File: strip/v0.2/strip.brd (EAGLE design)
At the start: 71 x 12 mm, 96 parts, among them IC1 LP2992, IC2 AUIRS2184S, IC3 MAX3051, IC4 OPA335, IC5 AUIRS2184S, IC6 AUIRS2184S, IC7 STM32F050CX, Q1 IRF7828, Q2 IRF7828, Q3 IRF7828, Q4 IRF7828, Q5 IRF7828, Q6 IRF7828

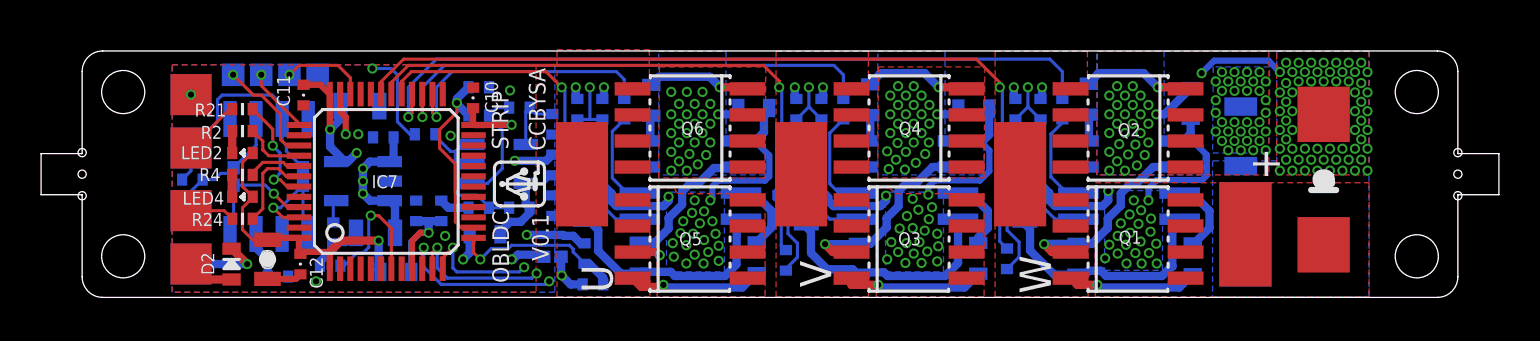
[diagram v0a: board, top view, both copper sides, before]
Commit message: Updated bootstrap circuit.
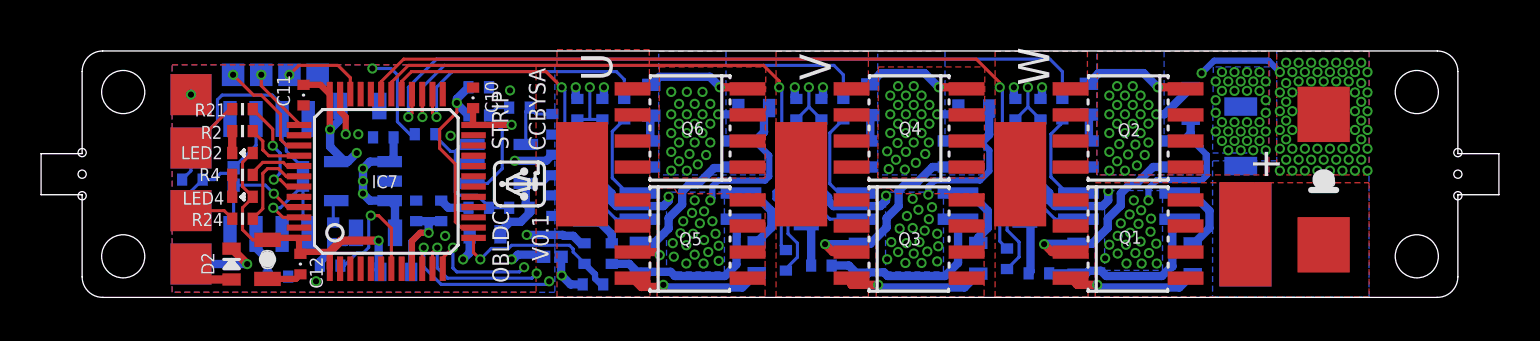
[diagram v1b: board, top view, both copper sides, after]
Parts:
- added R52, R53, R54: 2R, pel_dipol_comp:0402-RES
- D1, D3: value BAS21 -> BAT46WH
- R46, R47, R48, R49, R50, R51: value 10R -> 5R
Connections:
- new net N$1: D1.C, R52.P$2
- new net N$2: D4.C, R54.P$2
- new net N$3: D3.C, R53.P$2
- net U_VB: now also R52.P$1; no longer D1.C
- net V_VB: now also R53.P$1; no longer D3.C
- net W_VB: now also R54.P$1; no longer D4.C
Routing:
- net W_VB: track 12.2 -> 8.86 mm
- net V_VB: track 11.9 -> 8.98 mm
- net N$2: track 0.00 -> 2.83 mm
- net U_VB: track 11.8 -> 9.03 mm
- net N$3: track 0.00 -> 2.26 mm
- net N$1: track 0.00 -> 2.09 mm

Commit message: Updated bootstrap circuit
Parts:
- C23, C24, C25: value 1u -> 100nF
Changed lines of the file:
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@@
 <attribute name="PARTNO" value="*" x="20.5232" y="5.5332" size="1.778" layer="28" rot="MR90" display="off"/>
 </element>
-<element name="C23" library="pel_dipol_comp" package="0603-CAP" value="1u" x="23.114" y="1.909" smashed="yes" rot="MR90">
+<element name="C23" library="pel_dipol_comp" package="0603-CAP" value="100nF" x="23.114" y="1.909" smashed="yes" rot="MR90">
 <attribute name="NAME" x="23.5966" y="0.9438" size="0.635" layer="26" font="vector" ratio="16" rot="MR90"/>
 <attribute name="VALUE" x="21.59" y="0.7914" size="0.635" layer="28" font="vector" ratio="16" rot="MR90"/>
@@
 <attribute name="PARTNO" value="*" x="31.2674" y="5.3554" size="1.778" layer="28" rot="MR90" display="off"/>
 </element>
-<element name="C24" library="pel_dipol_comp" package="0603-CAP" value="1u" x="33.782" y="1.8582" smashed="yes" rot="MR90">
+<element name="C24" library="pel_dipol_comp" package="0603-CAP" value="100nF" x="33.782" y="1.8582" smashed="yes" rot="MR90">
 <attribute name="NAME" x="34.1884" y="0.893" size="0.635" layer="26" font="vector" ratio="16" rot="MR90"/>
 <attribute name="VALUE" x="32.258" y="0.7406" size="0.635" layer="28" font="vector" ratio="16" rot="MR90"/>
@@
 <attribute name="PARTNO" value="*" x="41.91" y="5.4824" size="1.778" layer="28" rot="MR90" display="off"/>
 </element>
-<element name="C25" library="pel_dipol_comp" package="0603-CAP" value="1u" x="44.4246" y="1.8582" smashed="yes" rot="MR90">
+<element name="C25" library="pel_dipol_comp" package="0603-CAP" value="100nF" x="44.4246" y="1.8582" smashed="yes" rot="MR90">
 <attribute name="NAME" x="44.9072" y="0.9692" size="0.635" layer="26" font="vector" ratio="16" rot="MR90"/>
 <attribute name="VALUE" x="42.9006" y="0.7406" size="0.635" layer="28" font="vector" ratio="16" rot="MR90"/>
@@
 </signal>
 </signals>
-<errors>
-</errors>
 </board>
 </drawing>

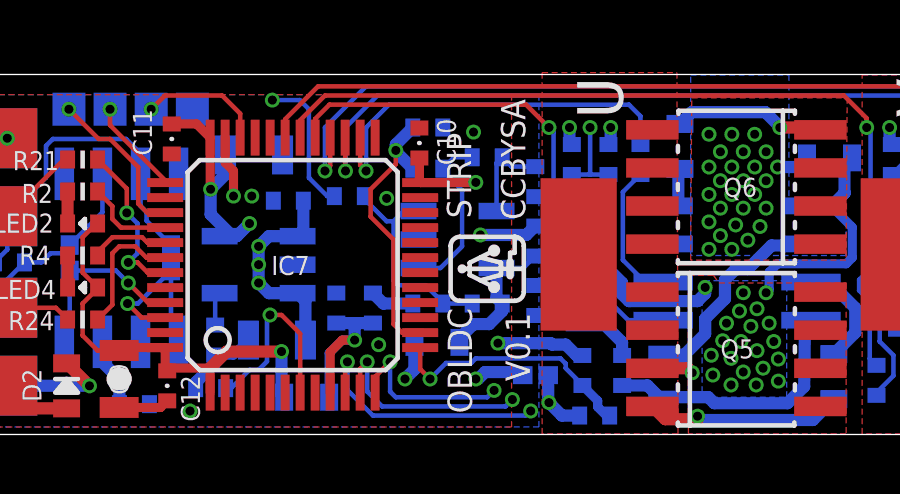
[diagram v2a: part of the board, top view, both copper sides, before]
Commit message: Updated current measurement circuit.
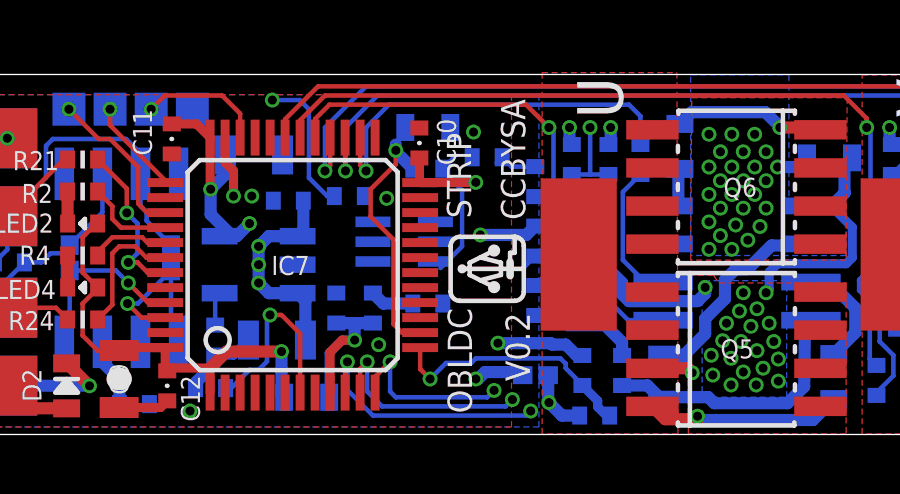
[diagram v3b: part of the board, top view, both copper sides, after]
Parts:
- removed IC4: OPA335, open-bldc:SOT23-5
- removed L1: (no value), res_cap:0603-IND
- removed R29: 7k7, pel_dipol_comp:0402-RES
- added U1: INA214AIDCKT, open-bldc:SOT65P210X110-6N
- C20: value 100nF/DNP -> 1uF/DNP; device pel_dipol_comp:0402-CAP -> pel_dipol_comp:0603-CAP
- R13: value 2k7 -> 1k5
- R27: value 660 -> 10
- R28: value 560 -> 10
- R45: value 0.005Ohm -> 0.002Ohm
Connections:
- removed net N$11: IC4.3, R27.P$1, R28.P$2, R29.P$2
- removed net N$12: IC4.4, R30.P$2, R31.P$2
- removed net N$9: C19.P$2, IC4.5, L1.P$1, R29.P$1
- new net CURRENTREF: IC7.15, R30.P$2, R31.P$2, U1.1
- new net INA21_INN: C20.P$1, R28.P$2, U1.5
- new net INA21_INP: C20.P$2, R27.P$1, U1.4
- net +3V3: now also C19.P$2, R31.P$1, U1.3; no longer L1.P$2
- net CURRENT: no longer C20.P$2
- net CURRENT_RAW: now also U1.6; no longer IC4.1, R31.P$1
- net GND: now also U1.2; no longer C20.P$1, IC4.2
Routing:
- net N$11: track 7.29 -> 0.00 mm
- net N$9: track 4.91 -> 0.00 mm
- net N$12: track 3.10 -> 0.00 mm
- net CURRENTREF: track 0.00 -> 1.50 mm
- net CURRENT_RAW: track 5.75 -> 4.42 mm
- net CURRENT: track 9.30 -> 8.50 mm
- net +3V3: track 28.7 -> 27.9 mm, vias 6 -> 5
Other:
- board text added: "V0.2"
- board text removed: "V0.1"

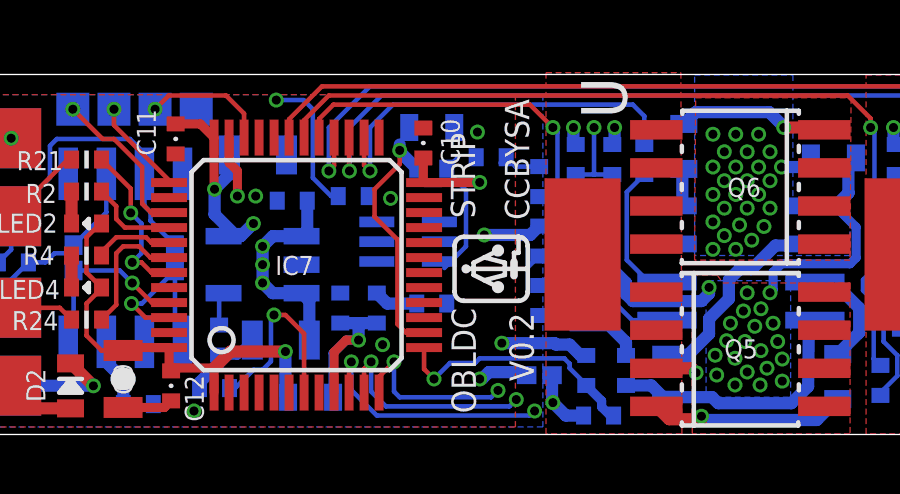
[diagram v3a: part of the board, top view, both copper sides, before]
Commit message: Wired the layout of the new current measurement.
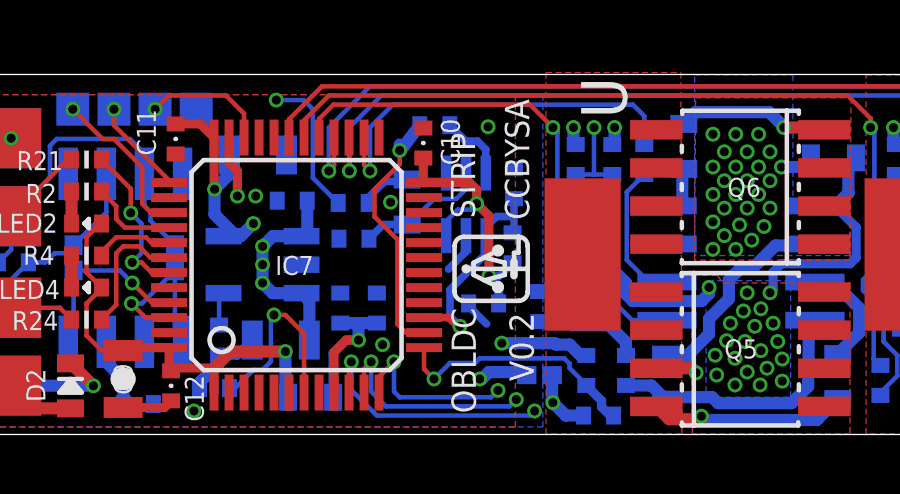
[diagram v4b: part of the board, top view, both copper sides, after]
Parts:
- C1: value 4µ7 -> 1u
- C23, C24, C25: value 100nF -> 1uF
- moved R28 3.37 mm to (12.7, 6.52)
- moved R31 3.10 mm to (18.0, 6.22), turned to 90 degrees
- moved C19 2.78 mm to (17.0, 4.37), turned to 180 degrees
- moved C20 2.62 mm to (14.5, 7.75), turned to 90 degrees
- moved U1 2.30 mm to (16.5, 7.67), turned to 90 degrees
- moved R37 1.45 mm to (15.4, 10.3)
- moved R30 0.84 mm to (18.1, 8.36), turned to 270 degrees
- moved R27 0.23 mm to (12.7, 7.72)
- moved R5 0.20 mm to (18.9, 4.26)
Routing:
- net +3V3: track 27.9 -> 34.1 mm, vias 5 -> 6
- net CURRENTREF: track 1.50 -> 7.49 mm, vias 0 -> 1
- net INA21_INN: track 0.00 -> 4.45 mm
- net INA21_INP: track 0.00 -> 3.37 mm
- net CURRENT_RAW: track 4.42 -> 2.32 mm
- net GND: track 57.2 -> 56.1 mm, vias 76 -> 75

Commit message: Fixed some part descriptons.
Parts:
- D4: value BAS21 -> BAT46WH
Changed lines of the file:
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@@
 <attribute name="PARTNO" value="cap-tan-0603-1u" x="33.782" y="1.8582" size="1.778" layer="28" rot="MR90" display="off"/>
 </element>
-<element name="D4" library="pel_dipol_comp" package="SOD-123-DIO" value="BAS21" x="41.91" y="5.4824" smashed="yes" rot="MR90">
+<element name="D4" library="pel_dipol_comp" package="SOD-123-DIO" value="BAT46WH" x="41.91" y="5.4824" smashed="yes" rot="MR90">
 <attribute name="NAME" x="42.926" y="4.9998" size="0.635" layer="26" font="vector" ratio="16" rot="MR90"/>
 <attribute name="VALUE" x="43.688" y="4.0854" size="1.27" layer="28" ratio="10" rot="MR90"/>
@@
 </signal>
 </signals>
-<errors>
-</errors>
 </board>
 </drawing>

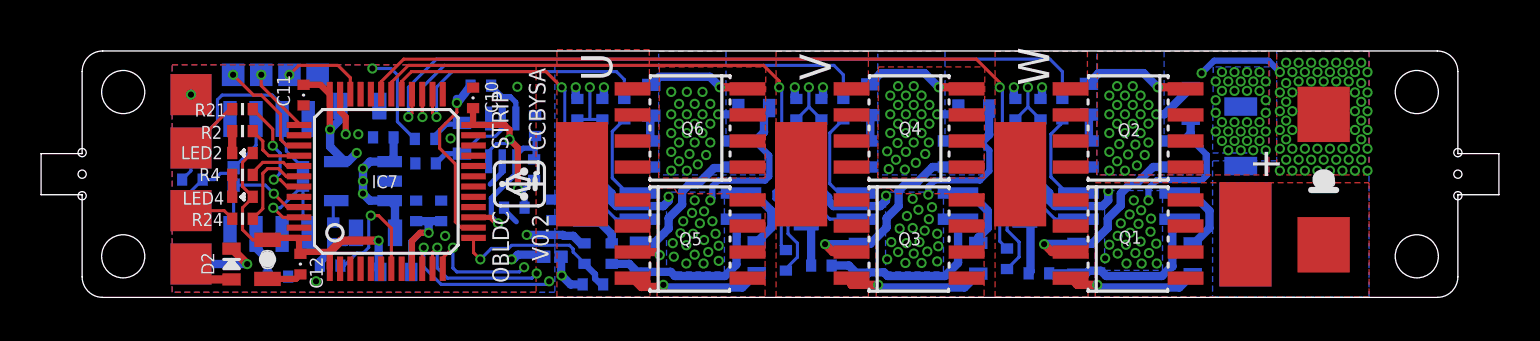
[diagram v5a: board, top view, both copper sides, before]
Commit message: Strip v0.2 layout after manufacturer review.
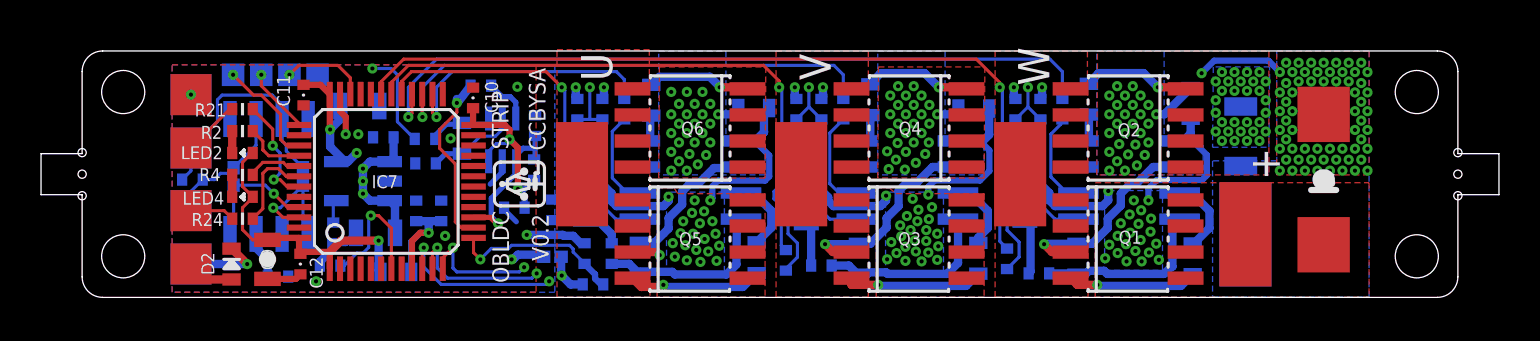
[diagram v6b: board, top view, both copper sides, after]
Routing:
- net PGND: vias 117 -> 113
- net BUSS+: vias 66 -> 69

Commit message: Corrected some component values.
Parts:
- C23, C24, C25: value 1uF -> 0.47uF
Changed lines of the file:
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@@
 <grid distance="1" unitdist="mil" unit="mm" style="dots" multiple="1" display="yes" altdistance="0.5" altunitdist="mil" altunit="mil"/>
 <layers>
-<layer number="1" name="Top" color="4" fill="1" visible="yes" active="yes"/>
+<layer number="1" name="Top" color="4" fill="1" visible="no" active="yes"/>
 <layer number="2" name="Route2" color="1" fill="3" visible="yes" active="yes"/>
 <layer number="3" name="Route3" color="4" fill="3" visible="no" active="no"/>
@@
 <layer number="19" name="Unrouted" color="6" fill="1" visible="yes" active="yes"/>
 <layer number="20" name="Dimension" color="15" fill="1" visible="yes" active="yes"/>
-<layer number="21" name="tPlace" color="7" fill="1" visible="yes" active="yes"/>
+<layer number="21" name="tPlace" color="7" fill="1" visible="no" active="yes"/>
 <layer number="22" name="bPlace" color="7" fill="1" visible="yes" active="yes"/>
-<layer number="23" name="tOrigins" color="15" fill="1" visible="yes" active="yes"/>
+<layer number="23" name="tOrigins" color="15" fill="1" visible="no" active="yes"/>
 <layer number="24" name="bOrigins" color="15" fill="1" visible="yes" active="yes"/>
 <layer number="25" name="tNames" color="7" fill="1" visible="no" active="yes"/>
@@
 <attribute name="PARTNO" value="*" x="20.5232" y="5.5332" size="1.778" layer="28" rot="MR90" display="off"/>
 </element>
-<element name="C23" library="pel_dipol_comp" package="0603-CAP" value="1uF" x="23.114" y="1.909" smashed="yes" rot="MR90">
+<element name="C23" library="pel_dipol_comp" package="0603-CAP" value="0.47uF" x="23.114" y="1.909" smashed="yes" rot="MR90">
 <attribute name="NAME" x="23.5966" y="0.9438" size="0.635" layer="26" font="vector" ratio="16" rot="MR90"/>
 <attribute name="VALUE" x="21.59" y="0.7914" size="0.635" layer="28" font="vector" ratio="16" rot="MR90"/>
@@
 <attribute name="PARTNO" value="*" x="31.2674" y="5.3554" size="1.778" layer="28" rot="MR90" display="off"/>
 </element>
-<element name="C24" library="pel_dipol_comp" package="0603-CAP" value="1uF" x="33.782" y="1.8582" smashed="yes" rot="MR90">
+<element name="C24" library="pel_dipol_comp" package="0603-CAP" value="0.47uF" x="33.782" y="1.8582" smashed="yes" rot="MR90">
 <attribute name="NAME" x="34.1884" y="0.893" size="0.635" layer="26" font="vector" ratio="16" rot="MR90"/>
 <attribute name="VALUE" x="32.258" y="0.7406" size="0.635" layer="28" font="vector" ratio="16" rot="MR90"/>
@@
 <attribute name="PARTNO" value="*" x="41.91" y="5.4824" size="1.778" layer="28" rot="MR90" display="off"/>
 </element>
-<element name="C25" library="pel_dipol_comp" package="0603-CAP" value="1uF" x="44.4246" y="1.8582" smashed="yes" rot="MR90">
+<element name="C25" library="pel_dipol_comp" package="0603-CAP" value="0.47uF" x="44.4246" y="1.8582" smashed="yes" rot="MR90">
 <attribute name="NAME" x="44.9072" y="0.9692" size="0.635" layer="26" font="vector" ratio="16" rot="MR90"/>
 <attribute name="VALUE" x="42.9006" y="0.7406" size="0.635" layer="28" font="vector" ratio="16" rot="MR90"/>
@@
 </signal>
 </signals>
-<errors>
-</errors>
 </board>
 </drawing>

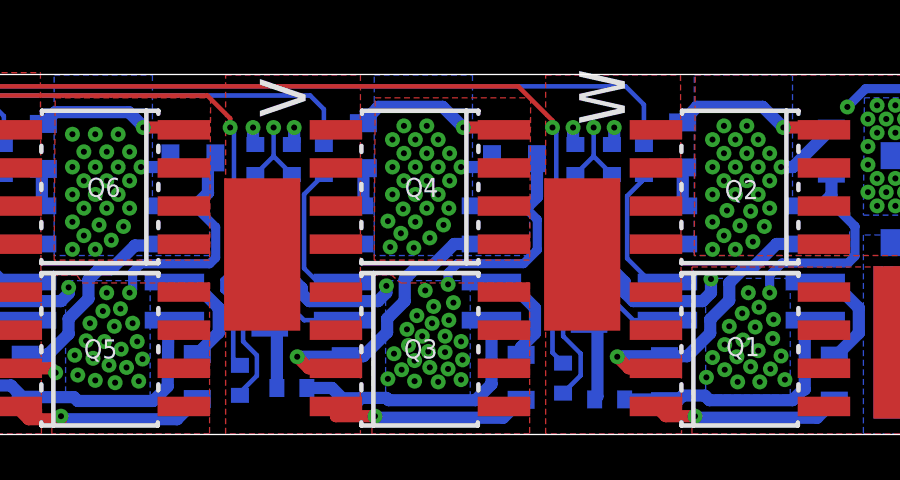
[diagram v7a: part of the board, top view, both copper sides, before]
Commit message: Pin COM of the IRS2184 driver is now connected to PGND... as it should.
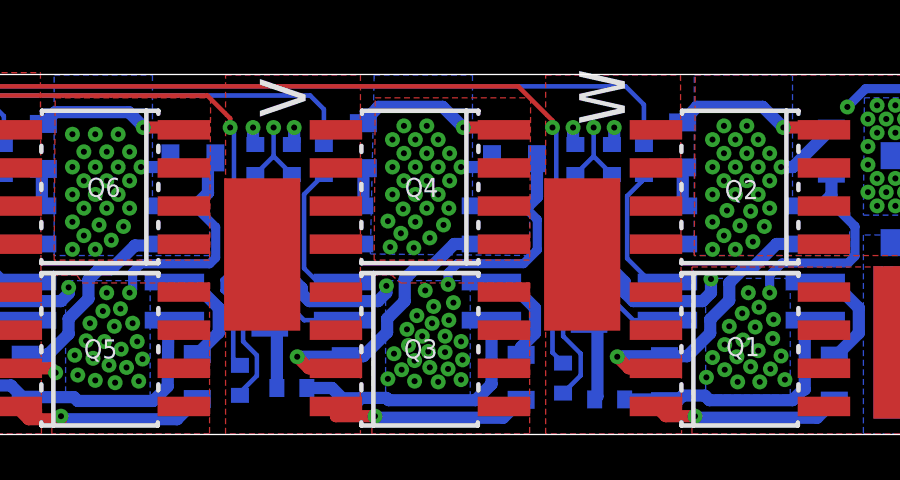
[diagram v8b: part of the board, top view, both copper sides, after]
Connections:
- net PGND: now also IC2.3, IC5.3, IC6.3
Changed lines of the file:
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@@
 <vertex x="39.9288" y="7.4128"/>
 <vertex x="39.9288" y="5.965"/>
-<vertex x="34.7472" y="5.965"/>
+<vertex x="34.6202" y="6.0158"/>
 </polygon>
 <polygon width="0.1524" layer="1" thermals="no">
@@
 <wire x1="49.9872" y1="10.1948" x2="48.7078" y2="8.9154" width="0.4064" layer="16"/>
 <wire x1="48.7078" y1="8.9154" x2="48.3108" y2="8.9154" width="0.4064" layer="16"/>
+<contactref element="IC2" pad="3"/>
+<contactref element="IC5" pad="3"/>
+<contactref element="IC6" pad="3"/>
 </signal>
 <signal name="CAN_H">
